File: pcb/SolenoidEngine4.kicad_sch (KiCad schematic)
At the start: 0 parts

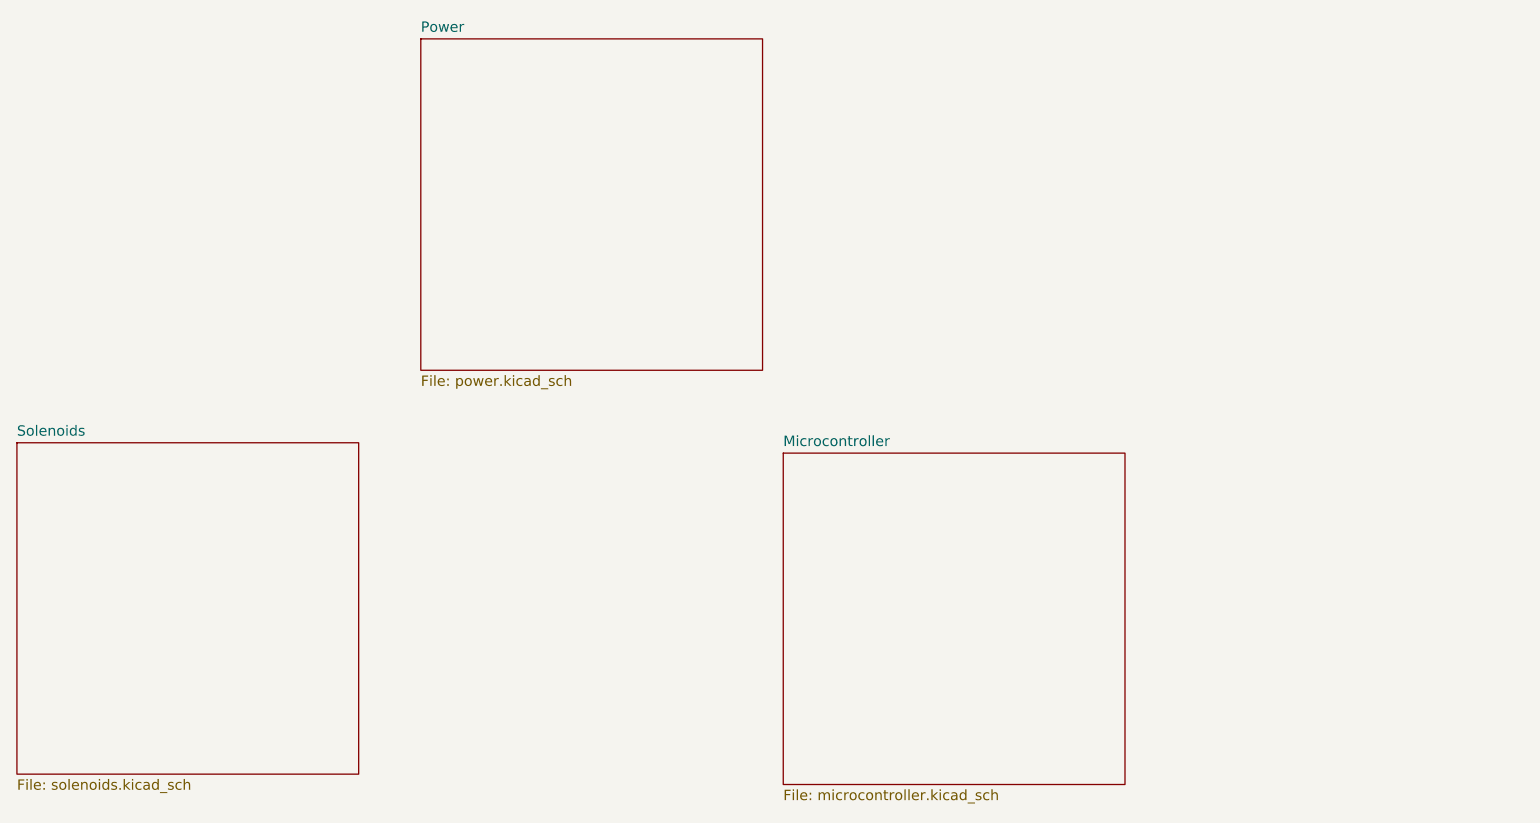
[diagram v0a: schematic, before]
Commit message: Create STM32 project, expand ADC and GPIO schematic
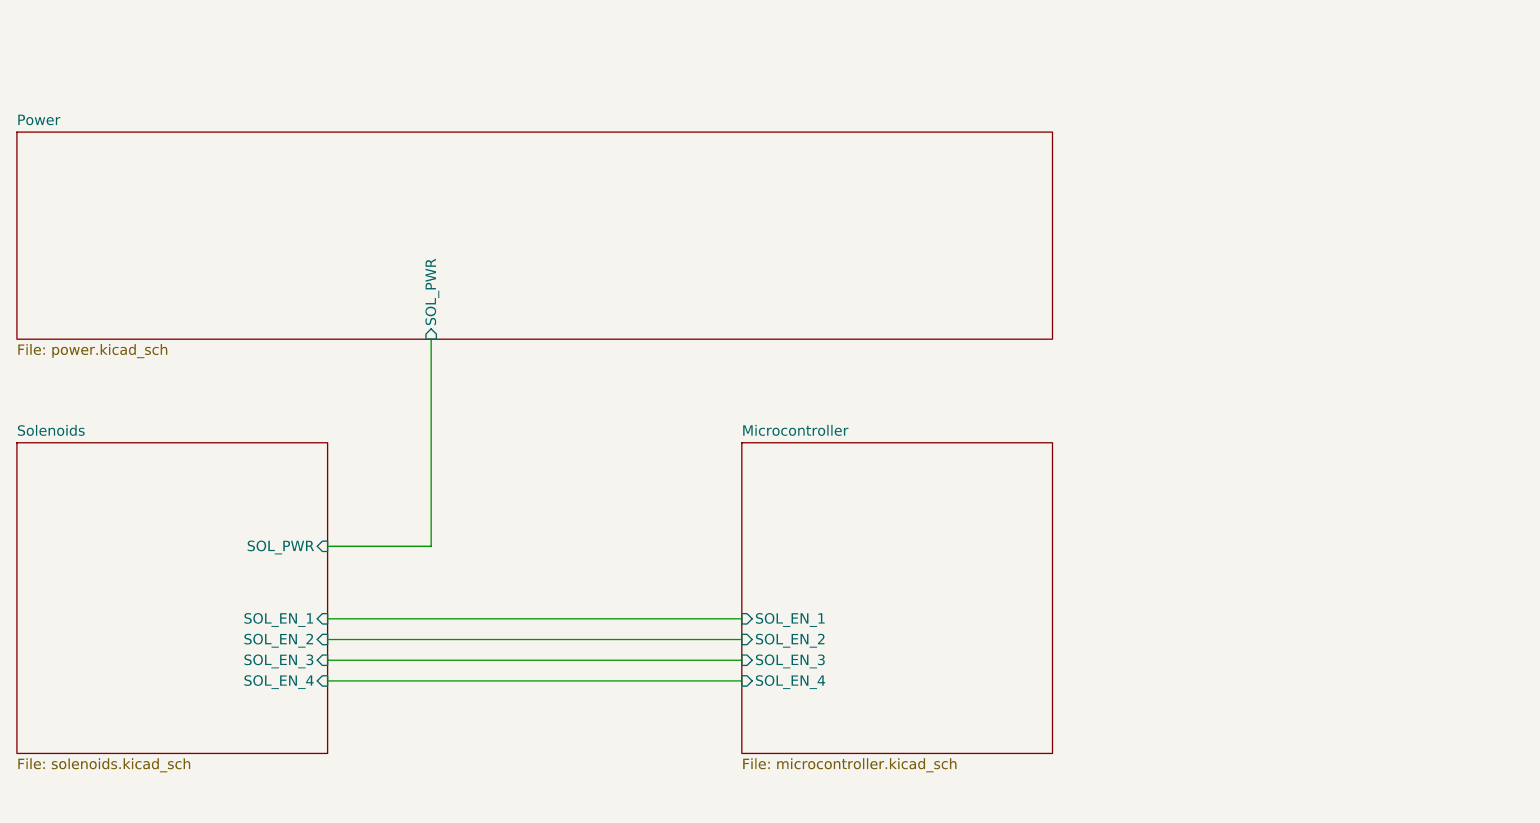
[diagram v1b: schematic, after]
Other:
- sheet Microcontroller ports: added SOL_EN_1, SOL_EN_2, SOL_EN_3, SOL_EN_4; removed none
- sheet Power ports: added SOL_PWR; removed none
- sheet Solenoids ports: added SOL_EN_1, SOL_EN_2, SOL_EN_3, SOL_EN_4, SOL_PWR; removed none
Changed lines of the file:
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@@
 	(generator_version "10.0")
 	(paper "A4")
+	(wire
+		(pts
+			(xy 101.6 97.79) (xy 152.4 97.79)
+		)
+		(stroke
+			(width 0)
+			(type default)
+		)
+	)
+	(wire
+		(pts
+			(xy 101.6 88.9) (xy 114.3 88.9)
+		)
+		(stroke
+			(width 0)
+			(type default)
+		)
+	)
+	(wire
+		(pts
+			(xy 114.3 88.9) (xy 114.3 63.5)
+		)
+		(stroke
+			(width 0)
+			(type default)
+		)
+	)
+	(wire
+		(pts
+			(xy 101.6 105.41) (xy 152.4 105.41)
+		)
+		(stroke
+			(width 0)
+			(type default)
+		)
+	)
+	(wire
+		(pts
+			(xy 101.6 100.33) (xy 152.4 100.33)
+		)
+		(stroke
+			(width 0)
+			(type default)
+		)
+	)
+	(wire
+		(pts
+			(xy 101.6 102.87) (xy 152.4 102.87)
+		)
+		(stroke
+			(width 0)
+			(type default)
+		)
+	)
 	(sheet
-		(at 157.48 77.47)
-		(size 41.91 40.64)
+		(at 152.4 76.2)
+		(size 38.1 38.1)
 		(exclude_from_sim no)
 		(in_bom yes)
@@
 			(width 0.1524)
 			(type solid)
+			(color 0 0 0 1)
 		)
 		(fill
-			(color 0 0 0 0)
+			(color 192 159 192 1)
 		)
 		(property "Sheetname" "Microcontroller"
-			(at 157.48 76.7584 0)
+			(at 152.4 75.4884 0)
 			(show_name no)
 			(do_not_autoplace no)
@@
 		)
 		(property "Sheetfile" "microcontroller.kicad_sch"
-			(at 157.48 118.6946 0)
+			(at 152.4 114.8846 0)
 			(show_name no)
 			(do_not_autoplace no)
@@
 		)
 		(property "Field2" ""
-			(at 157.48 77.47 0)
+			(at 152.4 76.2 0)
 			(hide yes)
 			(show_name no)
@@
 					(size 1.27 1.27)
 				)
+			)
+		)
+		(pin "SOL_EN_2" input
+			(at 152.4 100.33 180)
+			(effects
+				(font
+					(size 1.27 1.27)
+				)
+				(justify left)
+			)
+		)
+		(pin "SOL_EN_3" input
+			(at 152.4 102.87 180)
+			(effects
+				(font
+					(size 1.27 1.27)
+				)
+				(justify left)
+			)
+		)
+		(pin "SOL_EN_1" input
+			(at 152.4 97.79 180)
+			(effects
+				(font
+					(size 1.27 1.27)
+				)
+				(justify left)
+			)
+		)
+		(pin "SOL_EN_4" input
+			(at 152.4 105.41 180)
+			(effects
+				(font
+					(size 1.27 1.27)
+				)
+				(justify left)
 			)
 		)
@@
 	)
 	(sheet
-		(at 113.03 26.67)
-		(size 41.91 40.64)
+		(at 63.5 38.1)
+		(size 127 25.4)
 		(exclude_from_sim no)
 		(in_bom yes)
@@
 			(width 0.1524)
 			(type solid)
+			(color 0 0 0 1)
 		)
 		(fill
-			(color 0 0 0 0)
+			(color 1 192 0 1)
 		)
 		(property "Sheetname" "Power"
-			(at 113.03 25.9584 0)
+			(at 63.5 37.3884 0)
 			(show_name no)
 			(do_not_autoplace no)
@@
 		)
 		(property "Sheetfile" "power.kicad_sch"
-			(at 113.03 67.8946 0)
+			(at 63.5 64.0846 0)
 			(show_name no)
 			(do_not_autoplace no)
@@
 				)
 				(justify left top)
+			)
+		)
+		(pin "SOL_PWR" input
+			(at 114.3 63.5 270)
+			(effects
+				(font
+					(size 1.27 1.27)
+				)
+				(justify left)
 			)
 		)
@@
 	(sheet
 		(at 63.5 76.2)
-		(size 41.91 40.64)
+		(size 38.1 38.1)
 		(exclude_from_sim no)
 		(in_bom yes)
@@
 			(width 0.1524)
 			(type solid)
+			(color 0 0 0 1)
 		)
 		(fill
-			(color 0 0 0 0)
+			(color 189 192 0 1)
 		)
 		(property "Sheetname" "Solenoids"
@@
 		)
 		(property "Sheetfile" "solenoids.kicad_sch"
-			(at 63.5 117.4246 0)
+			(at 63.5 114.8846 0)
 			(show_name no)
 			(do_not_autoplace no)
@@
 			)
 		)
+		(pin "SOL_PWR" input
+			(at 101.6 88.9 0)
+			(effects
+				(font
+					(size 1.27 1.27)
+				)
+				(justify right)
+			)
+		)
+		(pin "SOL_EN_1" input
+			(at 101.6 97.79 0)
+			(effects
+				(font
+					(size 1.27 1.27)
+				)
+				(justify right)
+			)
+		)
+		(pin "SOL_EN_4" input
+			(at 101.6 105.41 0)
+			(effects
+				(font
+					(size 1.27 1.27)
+				)
+				(justify right)
+			)
+		)
+		(pin "SOL_EN_3" input
+			(at 101.6 102.87 0)
+			(effects
+				(font
+					(size 1.27 1.27)
+				)
+				(justify right)
+			)
+		)
+		(pin "SOL_EN_2" input
+			(at 101.6 100.33 0)
+			(effects
+				(font
+					(size 1.27 1.27)
+				)
+				(justify right)
+			)
+		)

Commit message: Main PCB nearly done, created resolver PCB, more STM32 work
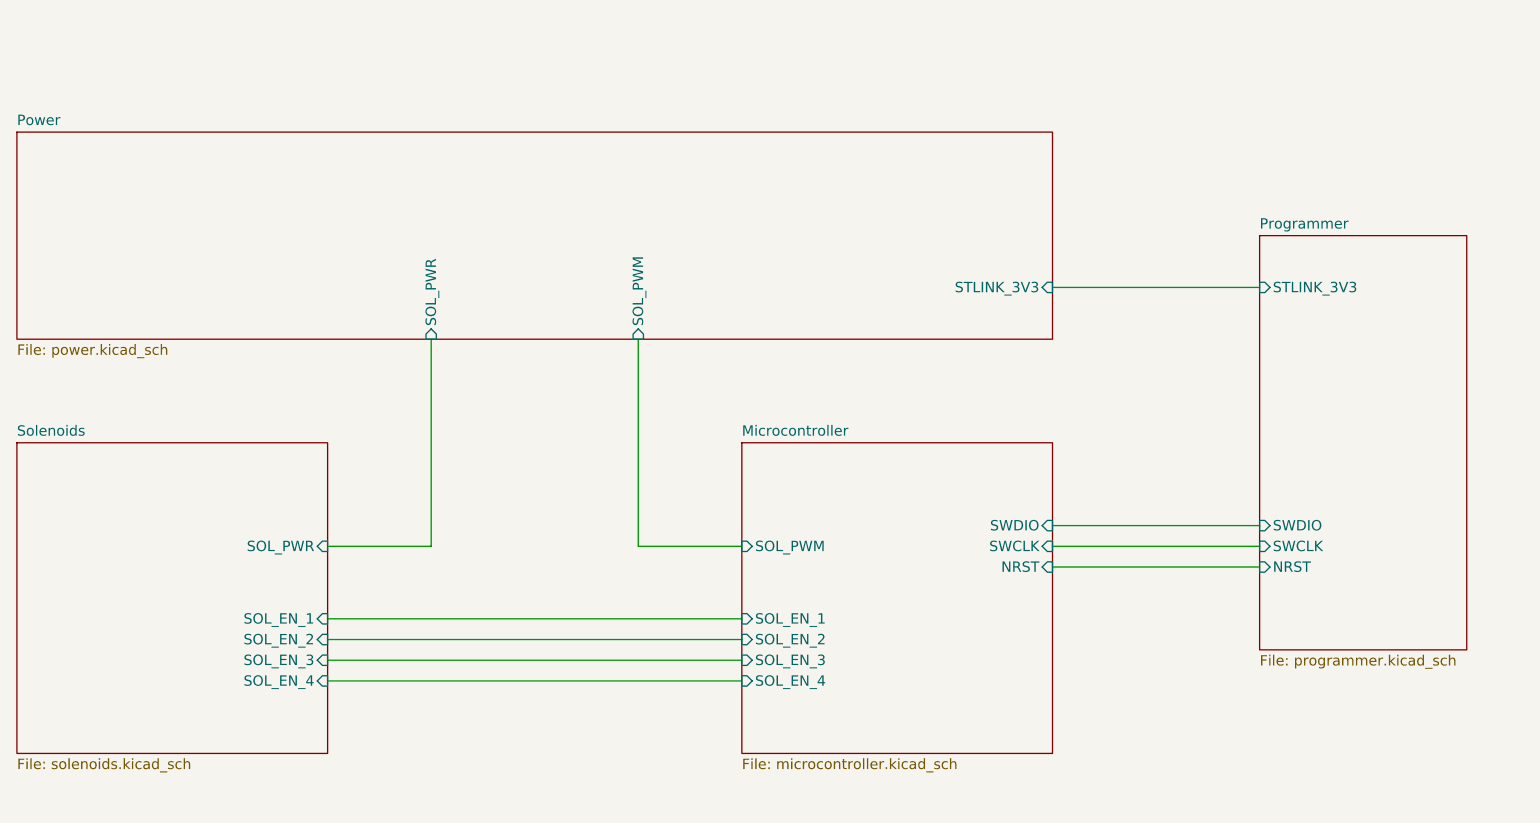
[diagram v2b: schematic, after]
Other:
- added sheet Programmer (programmer.kicad_sch)
- sheet Microcontroller ports: added NRST, SOL_PWM, SWCLK, SWDIO; removed none
- sheet Power ports: added SOL_PWM, STLINK_3V3; removed none
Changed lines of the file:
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@@
+	(wire
+		(pts
+			(xy 139.7 63.5) (xy 139.7 88.9)
+		)
+		(stroke
+			(width 0)
+			(type default)
+		)
+	)
+	(wire
+		(pts
+			(xy 190.5 57.15) (xy 215.9 57.15)
+		)
+		(stroke
+			(width 0)
+			(type default)
+		)
+	)
+	(wire
+		(pts
+			(xy 190.5 91.44) (xy 215.9 91.44)
+		)
+		(stroke
+			(width 0)
+			(type default)
+		)
+	)
 	(wire
 		(pts
@@
 	(wire
 		(pts
+			(xy 190.5 88.9) (xy 215.9 88.9)
+		)
+		(stroke
+			(width 0)
+			(type default)
+		)
+	)
+	(wire
+		(pts
 			(xy 101.6 105.41) (xy 152.4 105.41)
 		)
@@
 	(wire
 		(pts
+			(xy 139.7 88.9) (xy 152.4 88.9)
+		)
+		(stroke
+			(width 0)
+			(type default)
+		)
+	)
+	(wire
+		(pts
 			(xy 101.6 100.33) (xy 152.4 100.33)
 		)
@@
 			(width 0)
 			(type default)
+		)
+	)
+	(wire
+		(pts
+			(xy 190.5 86.36) (xy 215.9 86.36)
+		)
+		(stroke
+			(width 0)
+			(type default)
+		)
+	)
+	(sheet
+		(at 215.9 50.8)
+		(size 25.4 50.8)
+		(exclude_from_sim no)
+		(in_bom yes)
+		(on_board yes)
+		(dnp no)
+		(fields_autoplaced yes)
+		(stroke
+			(width 0.1524)
+			(type solid)
+		)
+		(fill
+			(color 166 246 255 1)
+		)
+		(property "Sheetname" "Programmer"
+			(at 215.9 50.0884 0)
+			(show_name no)
+			(do_not_autoplace no)
+			(effects
+				(font
+					(size 1.27 1.27)
+				)
+				(justify left bottom)
+			)
+		)
+		(property "Sheetfile" "programmer.kicad_sch"
+			(at 215.9 102.1846 0)
+			(show_name no)
+			(do_not_autoplace no)
+			(effects
+				(font
+					(size 1.27 1.27)
+				)
+				(justify left top)
+			)
+		)
+		(property "Field2" ""
+			(at 215.9 50.8 0)
+			(hide yes)
+			(show_name no)
+			(do_not_autoplace no)
+			(effects
+				(font
+					(size 1.27 1.27)
+				)
+			)
+		)
+		(pin "SWDIO" input
+			(at 215.9 86.36 180)
+			(effects
+				(font
+					(size 1.27 1.27)
+				)
+				(justify left)
+			)
+		)
+		(pin "SWCLK" input
+			(at 215.9 88.9 180)
+			(effects
+				(font
+					(size 1.27 1.27)
+				)
+				(justify left)
+			)
+		)
+		(pin "NRST" input
+			(at 215.9 91.44 180)
+			(effects
+				(font
+					(size 1.27 1.27)
+				)
+				(justify left)
+			)
+		)
+		(pin "STLINK_3V3" input
+			(at 215.9 57.15 180)
+			(effects
+				(font
+					(size 1.27 1.27)
+				)
+				(justify left)
+			)
+		)
+		(instances
+			(project "SolenoidEngine4"
+				(path "/8f70d105-0009-40db-8e47-cace6f06f216"
+					(page "9")
+				)
+			)
 		)
 	)
@@
 			)
 		)
+		(pin "SOL_PWM" input
+			(at 152.4 88.9 180)
+			(effects
+				(font
+					(size 1.27 1.27)
+				)
+				(justify left)
+			)
+		)
+		(pin "SWCLK" input
+			(at 190.5 88.9 0)
+			(effects
+				(font
+					(size 1.27 1.27)
+				)
+				(justify right)
+			)
+		)
+		(pin "SWDIO" input
+			(at 190.5 86.36 0)
+			(effects
+				(font
+					(size 1.27 1.27)
+				)
+				(justify right)
+			)
+		)
+		(pin "NRST" input
+			(at 190.5 91.44 0)
+			(effects
+				(font
+					(size 1.27 1.27)
+				)
+				(justify right)
+			)
+		)
 		(instances
 			(project "SolenoidEngine4"
@@
 			)
 		)
+		(pin "SOL_PWM" input
+			(at 139.7 63.5 270)
+			(effects
+				(font
+					(size 1.27 1.27)
+				)
+				(justify left)
+			)
+		)
+		(pin "STLINK_3V3" input
+			(at 190.5 57.15 0)
+			(effects
+				(font
+					(size 1.27 1.27)
+				)
+				(justify right)
+			)
+		)
